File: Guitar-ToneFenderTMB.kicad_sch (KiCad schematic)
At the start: 12 parts, among them J1 Screw_Terminal_1x02, J2 Screw_Terminal_1x02, J3 Screw_Terminal_1x01

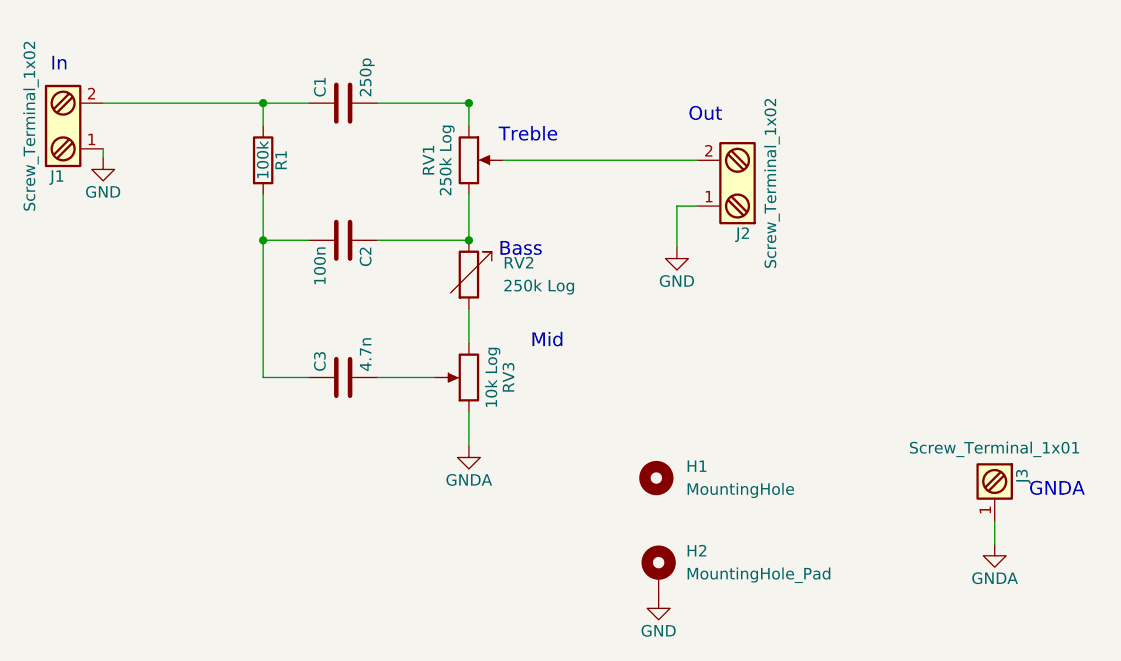
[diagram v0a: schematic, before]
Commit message: Fixed C3 value to 47n
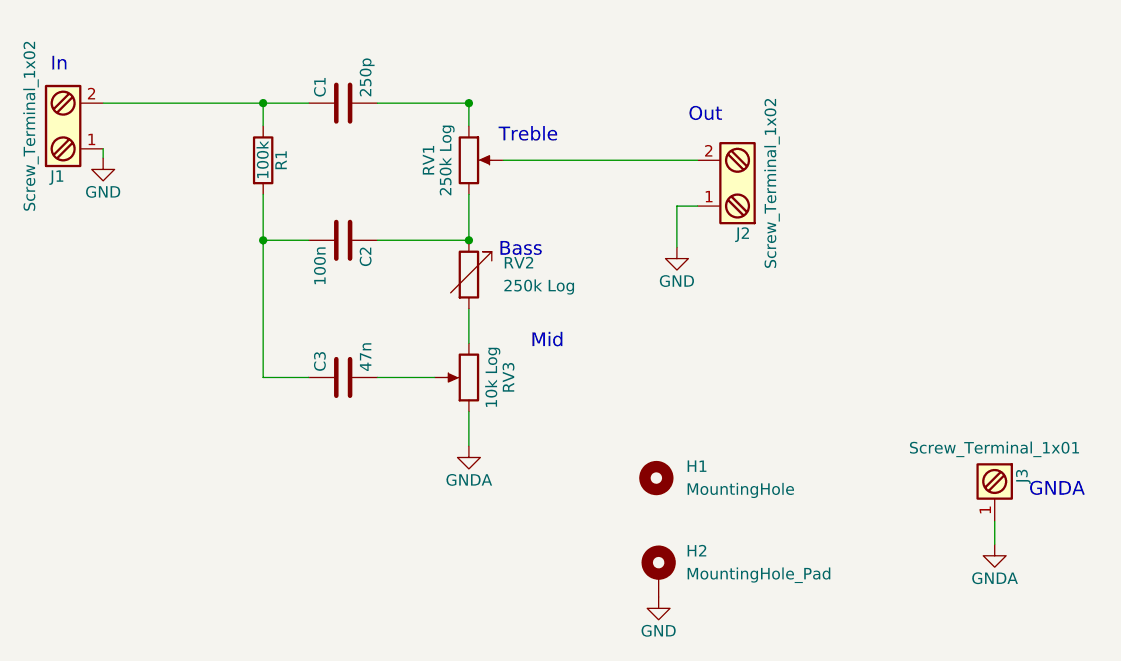
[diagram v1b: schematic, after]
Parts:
- C3: value 4.7n -> 47n
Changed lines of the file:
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@@
 			)
 		)
-		(property "Value" "4.7n"
+		(property "Value" "47n"
 			(at 100.33 84.455 0)
 			(effects
